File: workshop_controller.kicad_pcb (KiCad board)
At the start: 2 copper layers, 5 parts, among them J1 Conn_02x10_Odd_Even, J2 Conn_02x10_Odd_Even, U1 MPU-9250, U2 BME280, U3 MCP23S17_SS

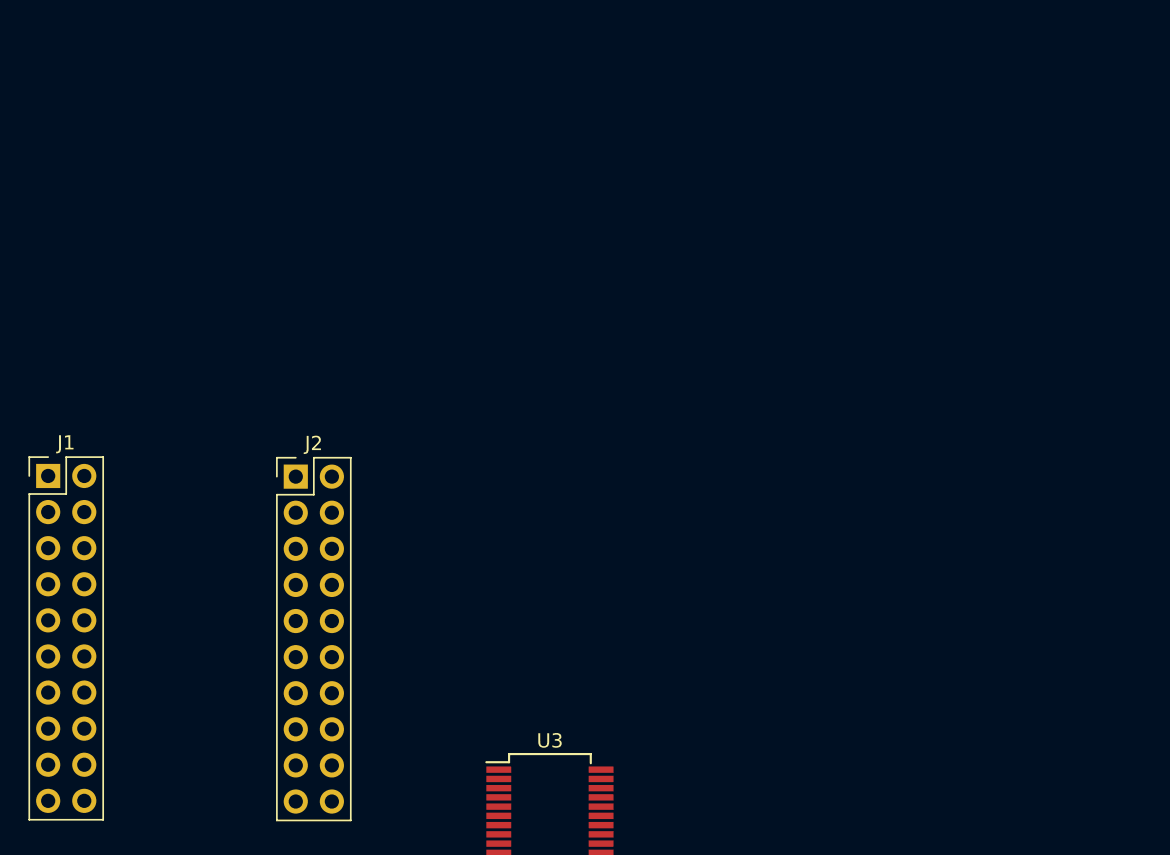
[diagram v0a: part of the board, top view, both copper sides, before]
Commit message: Add TFT Display connector
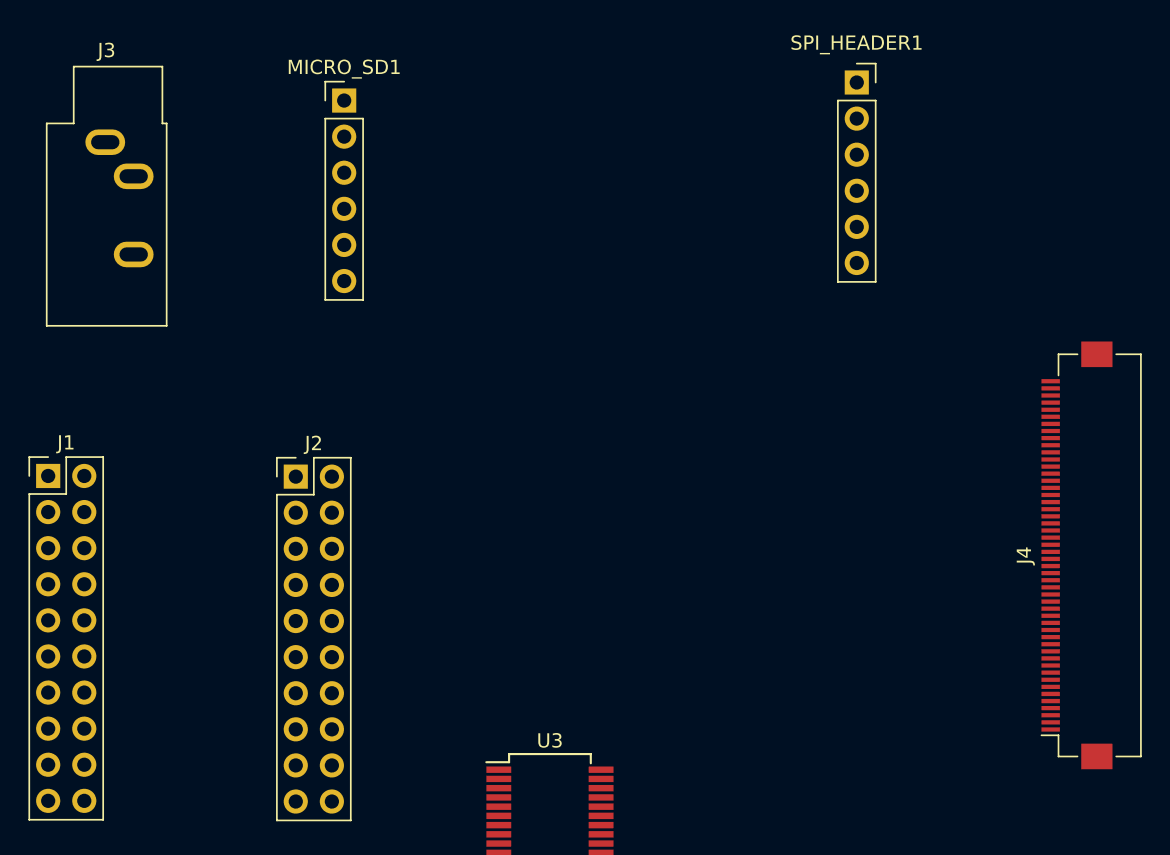
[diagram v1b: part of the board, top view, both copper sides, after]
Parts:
- added J3: AudioJack3, Connector_Audio:Jack_3.5mm_CUI_SJ1-3533NG_Horizontal, F.Cu at (106.1, 26.3)
- added J4: Conn_01x08, Connector_FFC-FPC:Hirose_FH12-50S-0.5SH_1x50-1MP_P0.50mm_Horizontal, F.Cu at (174.5, 55.4)
- added MICRO_SD1: Conn_01x06_Male, Connector_PinHeader_2.54mm:PinHeader_1x06_P2.54mm_Vertical, F.Cu at (122.9, 23.4)
- added SPI_HEADER1: Conn_01x06_Female, Connector_PinSocket_2.54mm:PinSocket_1x06_P2.54mm_Vertical, F.Cu at (159.0, 22.1)
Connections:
- U1 pad 23: /PIN_18 -> /PIN_27
- U1 pad 24: /PIN_23 -> /PIN_25
- U1 pad 9: /PIN_19 -> Net-(U1-Pad9)
- U2 pad 3: /PIN_19 -> /PIN_25
- U2 pad 4: /PIN_18 -> /PIN_27
- U2 pad 5: /PIN_23 -> Net-(U2-Pad5)

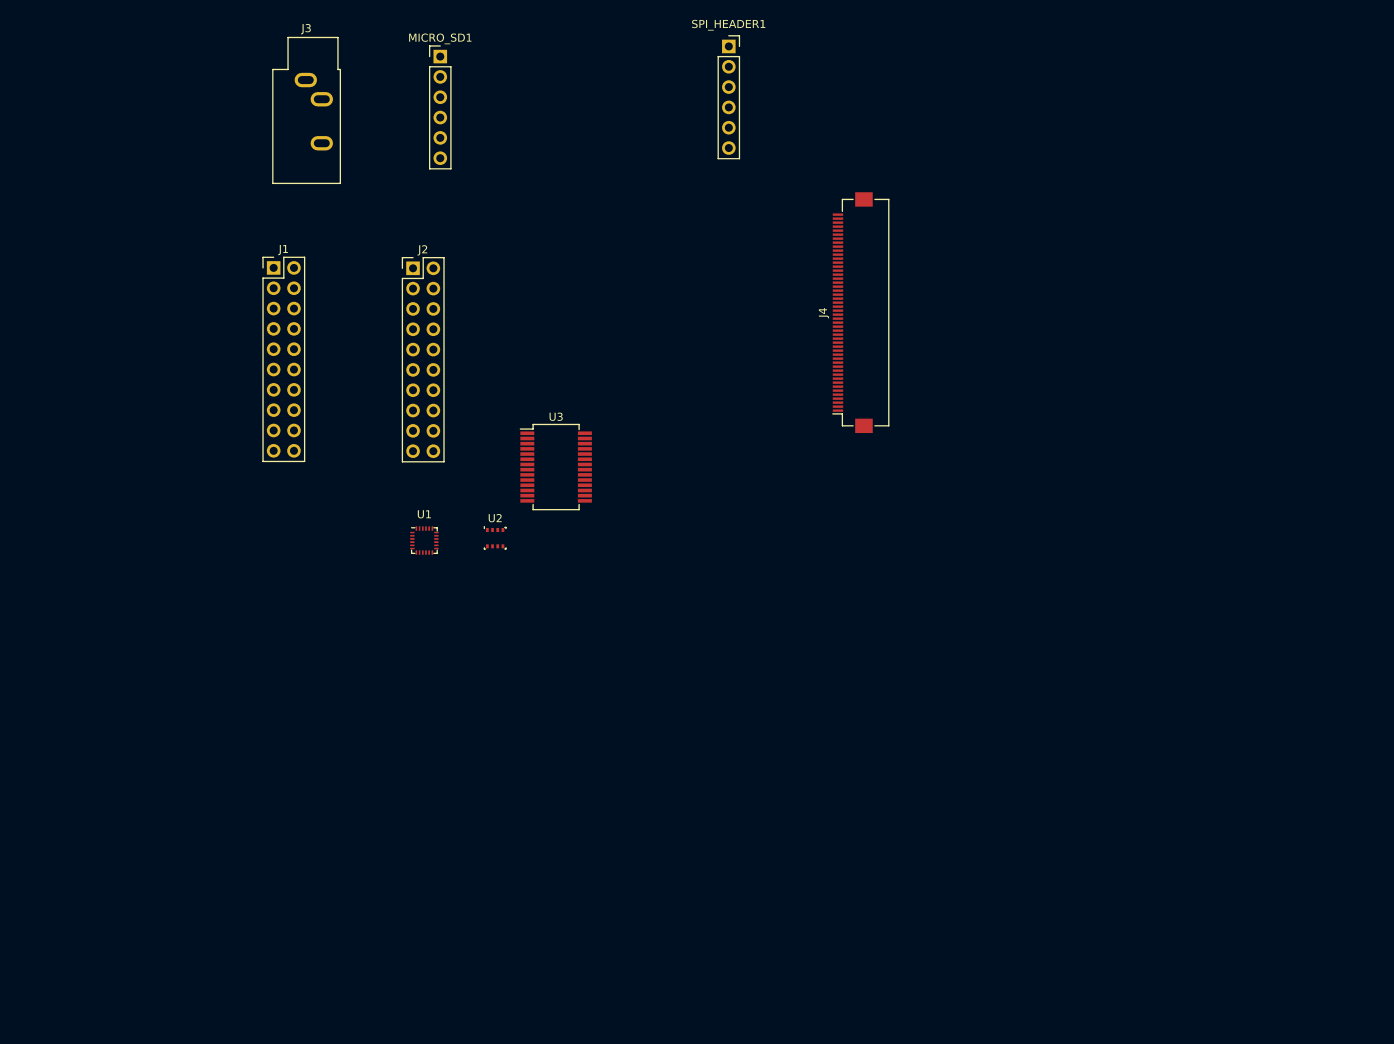
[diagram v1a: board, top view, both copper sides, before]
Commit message: Use correct symbol for FFC
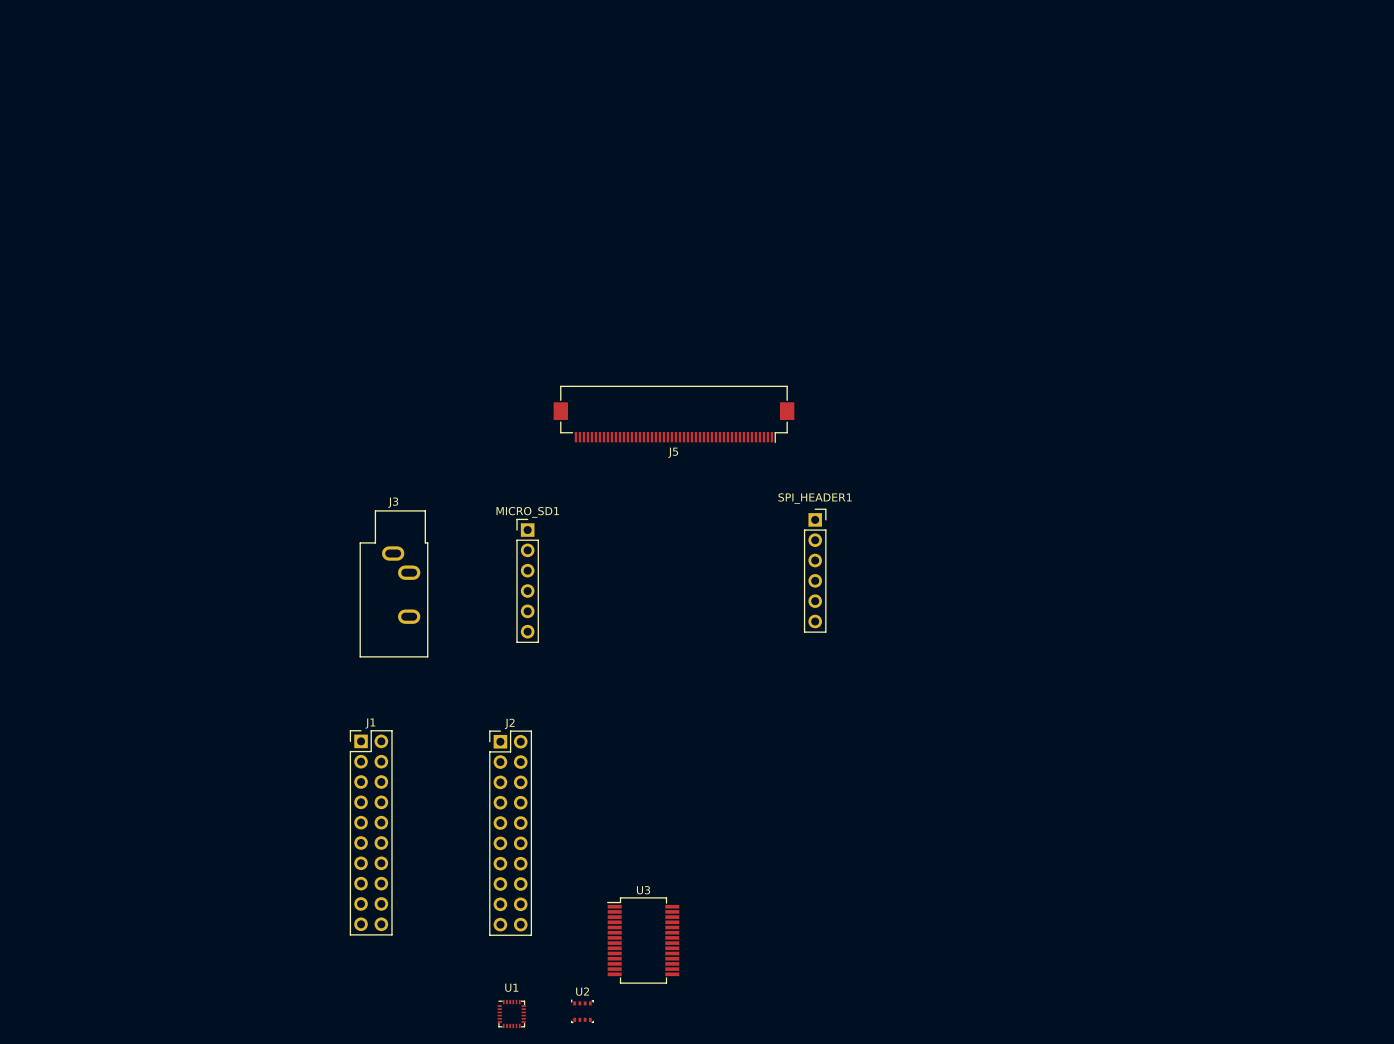
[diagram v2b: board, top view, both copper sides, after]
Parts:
- removed J4: Conn_01x08, Connector_FFC-FPC:Hirose_FH12-50S-0.5SH_1x50-1MP_P0.50mm_Horizontal
- added J5: Conn_02x25_Odd_Even, Connector_FFC-FPC:Hirose_FH12-50S-0.5SH_1x50-1MP_P0.50mm_Horizontal, F.Cu at (152.1, 69.1)
- moved U1 60.2 mm to (131.9, 143.0)
- moved J2 60.2 mm to (130.5, 109.0)
- moved J3 60.2 mm to (117.0, 85.5)
- moved MICRO_SD1 60.2 mm to (133.9, 82.5)
- moved U3 60.2 mm to (148.3, 133.9)
- moved J1 60.2 mm to (113.0, 109.0)
- moved U2 60.2 mm to (140.7, 142.7)
- moved SPI_HEADER1 60.2 mm to (169.8, 81.3)
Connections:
- J2 pad 19: /PIN_SDO -> /PIN_23

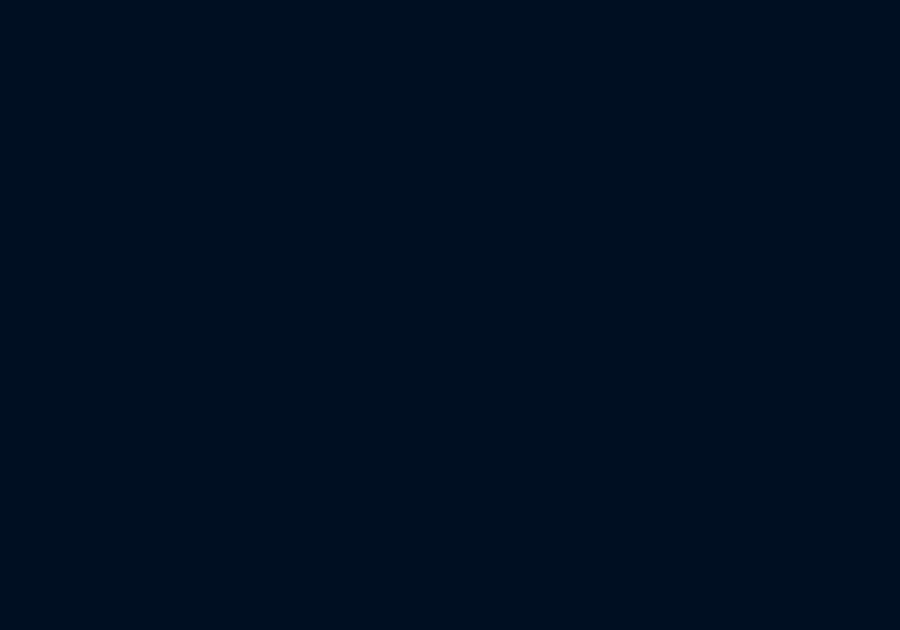
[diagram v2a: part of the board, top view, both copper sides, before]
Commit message: Connect mpu9250
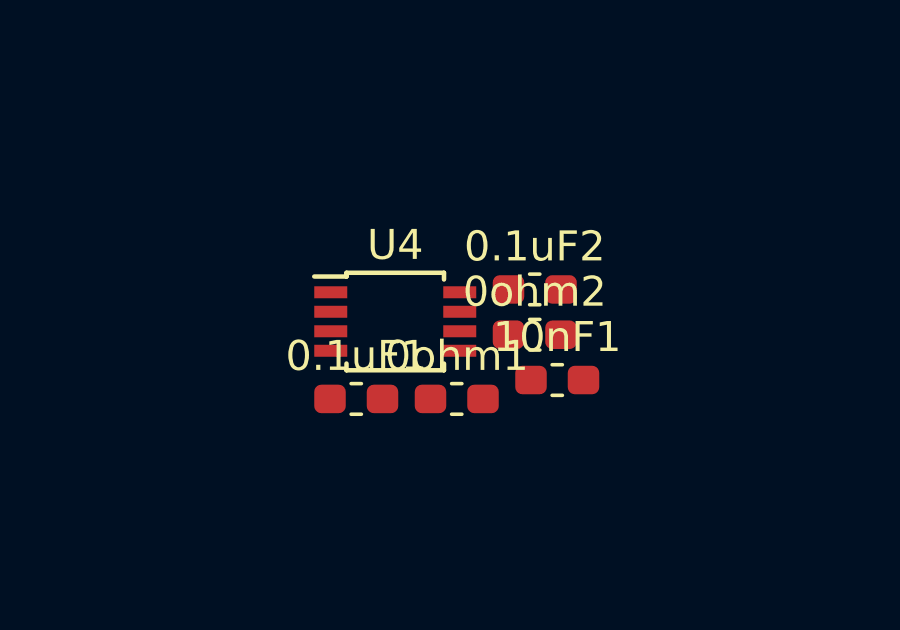
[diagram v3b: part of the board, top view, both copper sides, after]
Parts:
- added 0.1uF1: C_Small, Capacitor_SMD:C_0603_1608Metric_Pad1.05x0.95mm_HandSolder, F.Cu at (156.6, 114.6)
- added 0.1uF2: C_Small, Capacitor_SMD:C_0603_1608Metric_Pad1.05x0.95mm_HandSolder, F.Cu at (162.6, 111.0)
- added 0ohm1: R_Small, Resistor_SMD:R_0603_1608Metric_Pad1.05x0.95mm_HandSolder, F.Cu at (160.0, 114.6)
- added 0ohm2: R_Small, Resistor_SMD:R_0603_1608Metric_Pad1.05x0.95mm_HandSolder, F.Cu at (162.6, 112.5)
- added 10nF1: C_Small, Capacitor_SMD:C_0603_1608Metric_Pad1.05x0.95mm_HandSolder, F.Cu at (163.3, 114.0)
- added U4: LM4990MM, Package_SO:TSSOP-8_3x3mm_P0.65mm, F.Cu at (157.9, 112.1)
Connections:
- U1 pad 1: Net-(U1-Pad1) -> +3V3
- U1 pad 11: Net-(U1-Pad11) -> GND
- U1 pad 20: Net-(U1-Pad20) -> GND
- U1 pad 8: Net-(U1-Pad8) -> +3V3
